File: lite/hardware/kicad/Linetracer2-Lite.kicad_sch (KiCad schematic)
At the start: 31 parts, among them J1 BATTERY (AA x3, XH 2P), M1 LEFT motor FA-130RA, M2 RIGHT motor FA-130RA, Q1 2SC1815-GR, SW1 START, U1 XIAO ESP32C6, U2 AE-TC78H653FTG

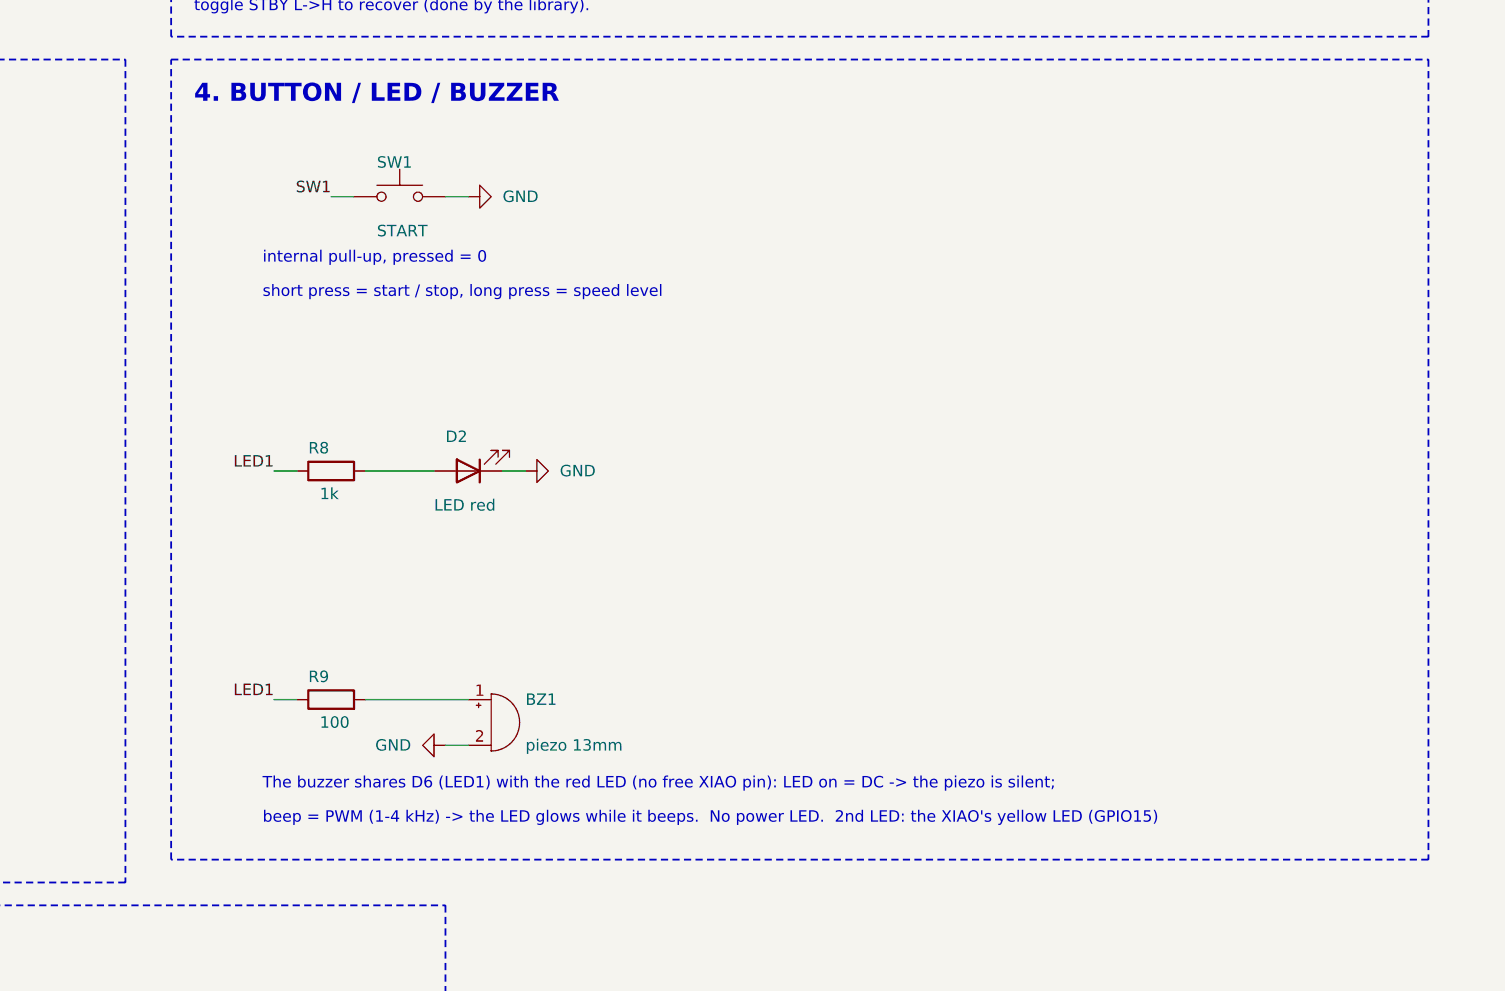
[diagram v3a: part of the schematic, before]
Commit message: ブザーを START ボタンのピン（D4）へ移し（R10 を追加）、ギヤボックスをデータシートで見直した
- ブザー: D6（赤 LED と共用）→ D4（START と共用）。ボタンは R10 1kΩ、圧電は R9 100Ω を通す。
  圧電は直流を通さないのでボタンはふつうに読め、押したままでも鳴る。LED は D6 を単独で使える。
  ソフトの beep() は D4 を一瞬 PWM の出力にしてから入力に戻す
- 基板: R10 を足して配置・配線をやり直し（DRC / ERC 0、ビア 0、配線 625 mm）。手順 ③ は あか 3 本
- ギヤボックス: FA-130 の公差（軸の出っぱり 9.5 ±0.5、ガタ 0.4）で軸の先とピニオンが外かべに当たりうる
  → 外かべに逃げ穴 φ6.5、壁を前へ 3 mm（check_shaft_wall、逃げ穴なしで検出できることも確認）。
  モーターはツメの摩擦だけで内側へずれうる → デッキの下にリブ（0.3 mm の面取り付き）。
  ピニオンを歯の形（8T）で描く
- 図: hardware/mechanical/gearbox_review.png（scripts/gearbox_figure.py）
- 出力を作り直した（Gerber・BOM・PDF・基板の 3D・手順の絵・ロボット全体の STL / GLB。干渉チェックは全部空）

Co-Authored-By: Claude Opus 5.5 <noreply@anthropic.com>
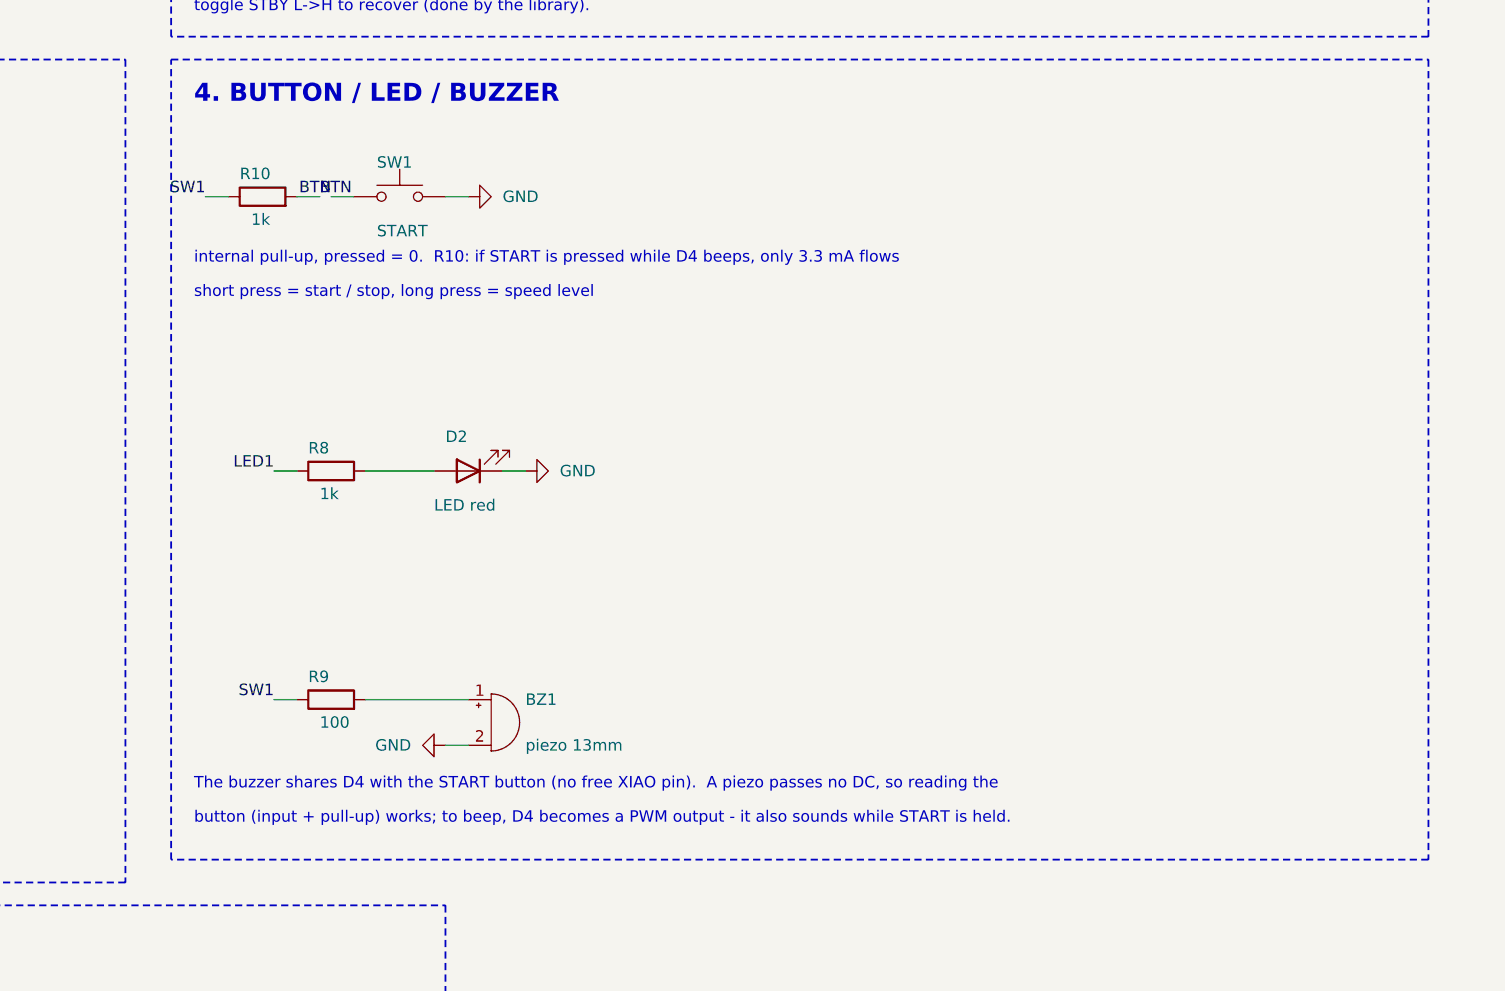
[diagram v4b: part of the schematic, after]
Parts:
- added R10: 1k, Resistor_THT:R_Axial_DIN0207_L6.3mm_D2.5mm_P10.16mm_Horizontal, symbol Device:R
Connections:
- net LED1: no longer R9.1
- net SW1: now also R9.1, R10.1; no longer SW1.1
- new net BTN: R10.2, SW1.1
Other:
- note added: "The buzzer shares D4 with the START button (no free XIAO pin). A piezo passes no DC, so reading the"
- note added: "button (input + pull-up) works; to beep, D4 becomes a PWM output - it also sounds while START is held."
- note added: "internal pull-up, pressed = 0. R10: if START is pressed while D4 beeps, only 3.3 mA flows"
- note removed: "The buzzer shares D6 (LED1) with the red LED (no free XIAO pin): LED on = DC -> the piezo is silent;"
- note removed: "beep = PWM (1-4 kHz) -> the LED glows while it beeps. No power LED. 2nd LED: the XIAO's yellow LED (GPIO15)"
- note removed: "internal pull-up, pressed = 0"

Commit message: Lite: 赤 LED をフルカラー LED PL9823 ×5 に、部品表を更新
- D2〜D6 = PL9823-F5（秋月 108411、NeoPixel 型）を D6 の 1 本の信号線でつなぐ。前 3 こ・うしろ 2 こを
  3.5 mm ずつずらして並べ、走っている間は線の位置を 5 だんかいで光らせる
- 電源は VSYS（裏の 1 本、2 列の間に横線）、C5 0.1 µF。赤 LED と R8 をなくした
- 足 1.27 mm の 4 本足は穴を前後に互いちがいに、● の点で GND（いちばん長い足）の穴を示す
- 背が高いので、つくる順番を ⑦ ボタン ⑧ ブザー ⑨ でんち ⑩ ドライバー ⑪ XIAO ⑫ フルカラー LED に付け直した
- DRC / ERC 0、ビア 0、干渉チェックはすべて空。手順の絵・3D・Gerber を作り直した
- ソフト: robot.led（色・fill・bar・count、value は今までどおり）、状態を色で表示、サンプル 07_rgb_led.py
- 部品表 lite/docs/bom.md を更新（1 台 約 ¥2,730、10 台分の秋月 ¥25,440）

Co-Authored-By: Claude Opus 5.5 <noreply@anthropic.com>
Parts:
- removed R8: 1k, Resistor_THT:R_Axial_DIN0207_L6.3mm_D2.5mm_P10.16mm_Horizontal, symbol Device:R
- added C5: 0.1uF, Capacitor_THT:C_Disc_D3.0mm_W2.0mm_P2.50mm, symbol Device:C
- added D3, D4, D5, D6: PL9823, Linetracer2:LED_PL9823_5mm, symbol Linetracer2:PL9823
- D2: value LED red -> PL9823; footprint LED_THT:LED_D3.0mm -> Linetracer2:LED_PL9823_5mm; symbol Device:LED -> Linetracer2:PL9823; Akizuki 111577 -> 108411 (PL9823-F5)
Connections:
- net GND: now also C5.2, D3.1 (GND), D4.1 (GND), D5.1 (GND), D6.1 (GND)
- net VSYS: now also D2.3 (VDD), C5.1, D3.3 (VDD), D4.3 (VDD), D5.3 (VDD), D6.3 (VDD)
- net at D2.2 (DO): now also D3.4 (DIN)
- net LED1 renamed RGB_DIN
- net RGB_DIN: now also D2.4 (DIN)
- new net: D5.2 (DO), D6.4 (DIN)
- new net: D4.2 (DO), D5.4 (DIN)
- new net: D3.2 (DO), D4.4 (DIN)
- no-connect marks 0 -> 1
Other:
- note added: "4. BUTTON / BUZZER / RGB LEDs"
- note added: "All 5 white at full power = about 0.3 A: the library limits the brightness."
- note added: "D2..D6 = PL9823 (NeoPixel type, 800 kHz, 24 bit per LED). Data from D6 (TX: the boot log may flash them once)."
- note added: "Linetracer2 Lite rev.L3 : XIAO ESP32C6 on pin headers, 3 x LBR-127HLD, 1 button, 1 buzzer, 5 RGB LEDs"
- note removed: "4. BUTTON / LED / BUZZER"
- note removed: "Linetracer2 Lite rev.L3 : XIAO ESP32C6 on pin headers, 3 x LBR-127HLD, 1 button, 1 LED, 1 buzzer"

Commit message: Lite: フルカラー LED を 6 こ・左右の端に、流れる光、テストパッド
- PL9823 ×6（D2〜D7）を基板の左右の端に 3 こずつ縦に。信号は D6 → 左のうしろ → 左の前 →
  前の端をわたって → 右の前 → 右のうしろ。電源 VSYS は裏の線（右の列の内側 → 前を横切って → 左の列の内側）
- 場所をあけるため Q1 を R7 の前へ（180° 回転）、抵抗の絵を真ん中へ、S3 の線を内側へ。C5 はなくした
- テストパッド 7 こ（GND・3V3・VSYS・S1・S2・S3・IR、表の SMD）＋ D1 の上のパッドに VBAT。
  値の表（README §4.9）と先生用プログラム 08_test_pads.py
- ソフト: robot.led.flow(左, 右) = 両側で光が前→うしろへ、その側の車輪の速さで流れる（走っているとき）。
  side() / count() / bar() も 6 こ用に。サンプル 07_rgb_led.py を直した
- DRC / ERC 0、ビア 0、干渉チェックはすべて空。手順の絵・3D・Gerber・部品表（1 台 約 ¥2,760）を作り直した

Co-Authored-By: Claude Opus 5.5 <noreply@anthropic.com>
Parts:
- removed C5: 0.1uF, Capacitor_THT:C_Disc_D3.0mm_W2.0mm_P2.50mm, symbol Device:C
- added D7: PL9823, Linetracer2:LED_PL9823_5mm, symbol Linetracer2:PL9823
- added TP1: GND, TestPoint:TestPoint_Pad_D1.5mm, symbol Connector:TestPoint
- added TP2: 3V3, TestPoint:TestPoint_Pad_D1.5mm, symbol Connector:TestPoint
- added TP3: VSYS, TestPoint:TestPoint_Pad_D1.5mm, symbol Connector:TestPoint
- added TP4: SENS1, TestPoint:TestPoint_Pad_D1.5mm, symbol Connector:TestPoint
- added TP5: SENS2, TestPoint:TestPoint_Pad_D1.5mm, symbol Connector:TestPoint
- added TP6: SENS3, TestPoint:TestPoint_Pad_D1.5mm, symbol Connector:TestPoint
- added TP7: LED_K, TestPoint:TestPoint_Pad_D1.5mm, symbol Connector:TestPoint
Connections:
- net +3V3: now also TP2.1
- net GND: now also D7.1 (GND), TP1.1
- net LED_K: now also TP7.1
- net SENS1: now also TP4.1
- net SENS2: now also TP5.1
- net SENS3: now also TP6.1
- net VSYS: now also D7.3 (VDD), TP3.1
- net at D6.2 (DO): now also D7.4 (DIN)
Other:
- note added: "(front -> rear). Data from D6 (TX: the boot log may flash them once). 6 x white = 0.36 A: the library limits it."
- note added: "6. TEST PADS (multimeter, black probe on GND)"
- note added: "D2..D7 = PL9823 (NeoPixel type, 800 kHz, 24 bit per LED): D2-D4 left side (rear -> front), D5-D7 right side"
- note added: "IR (LED_K): about 0.1 V while the IR LEDs are on (robot.sensors.leds(True)), about 2 V when off."
- note added: "Linetracer2 Lite rev.L3 : XIAO ESP32C6 on pin headers, 3 x LBR-127HLD, 1 button, 1 buzzer, 6 RGB LEDs"
- note added: "VBAT (D1 anode / J1 +) 3.6-4.8 V, VSYS = VBAT - 0.3 V (USB: 5 V), 3V3 = 3.3 V. S1-S3: white low, black ~3 V."
- note removed: "All 5 white at full power = about 0.3 A: the library limits the brightness."
- note removed: "D2..D6 = PL9823 (NeoPixel type, 800 kHz, 24 bit per LED). Data from D6 (TX: the boot log may flash them once)."
- note removed: "Linetracer2 Lite rev.L3 : XIAO ESP32C6 on pin headers, 3 x LBR-127HLD, 1 button, 1 buzzer, 5 RGB LEDs"
- moved on the sheet: D3, D4, D5, D6
